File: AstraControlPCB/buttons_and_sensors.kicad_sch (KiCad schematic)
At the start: 11 parts, among them CN13 4P JST ZH, CN14 4P JST ZH, CN5 4P JST ZH

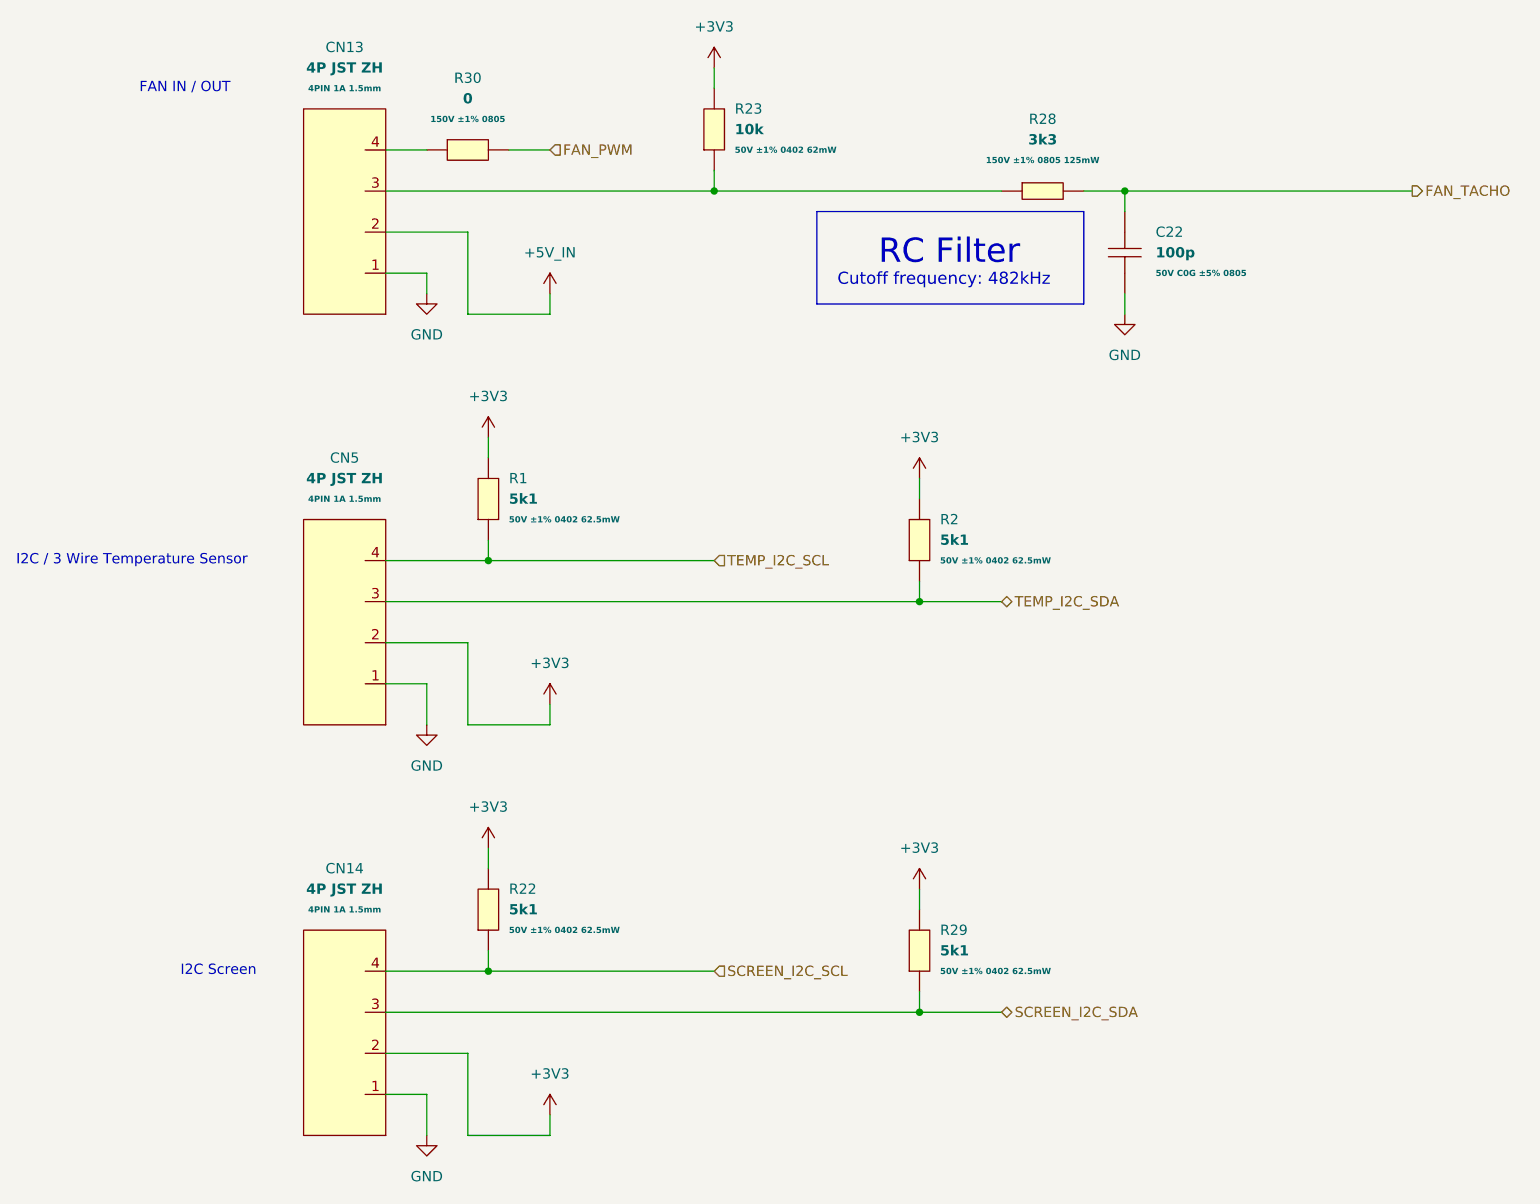
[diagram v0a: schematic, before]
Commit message: Remove plus minus symbol
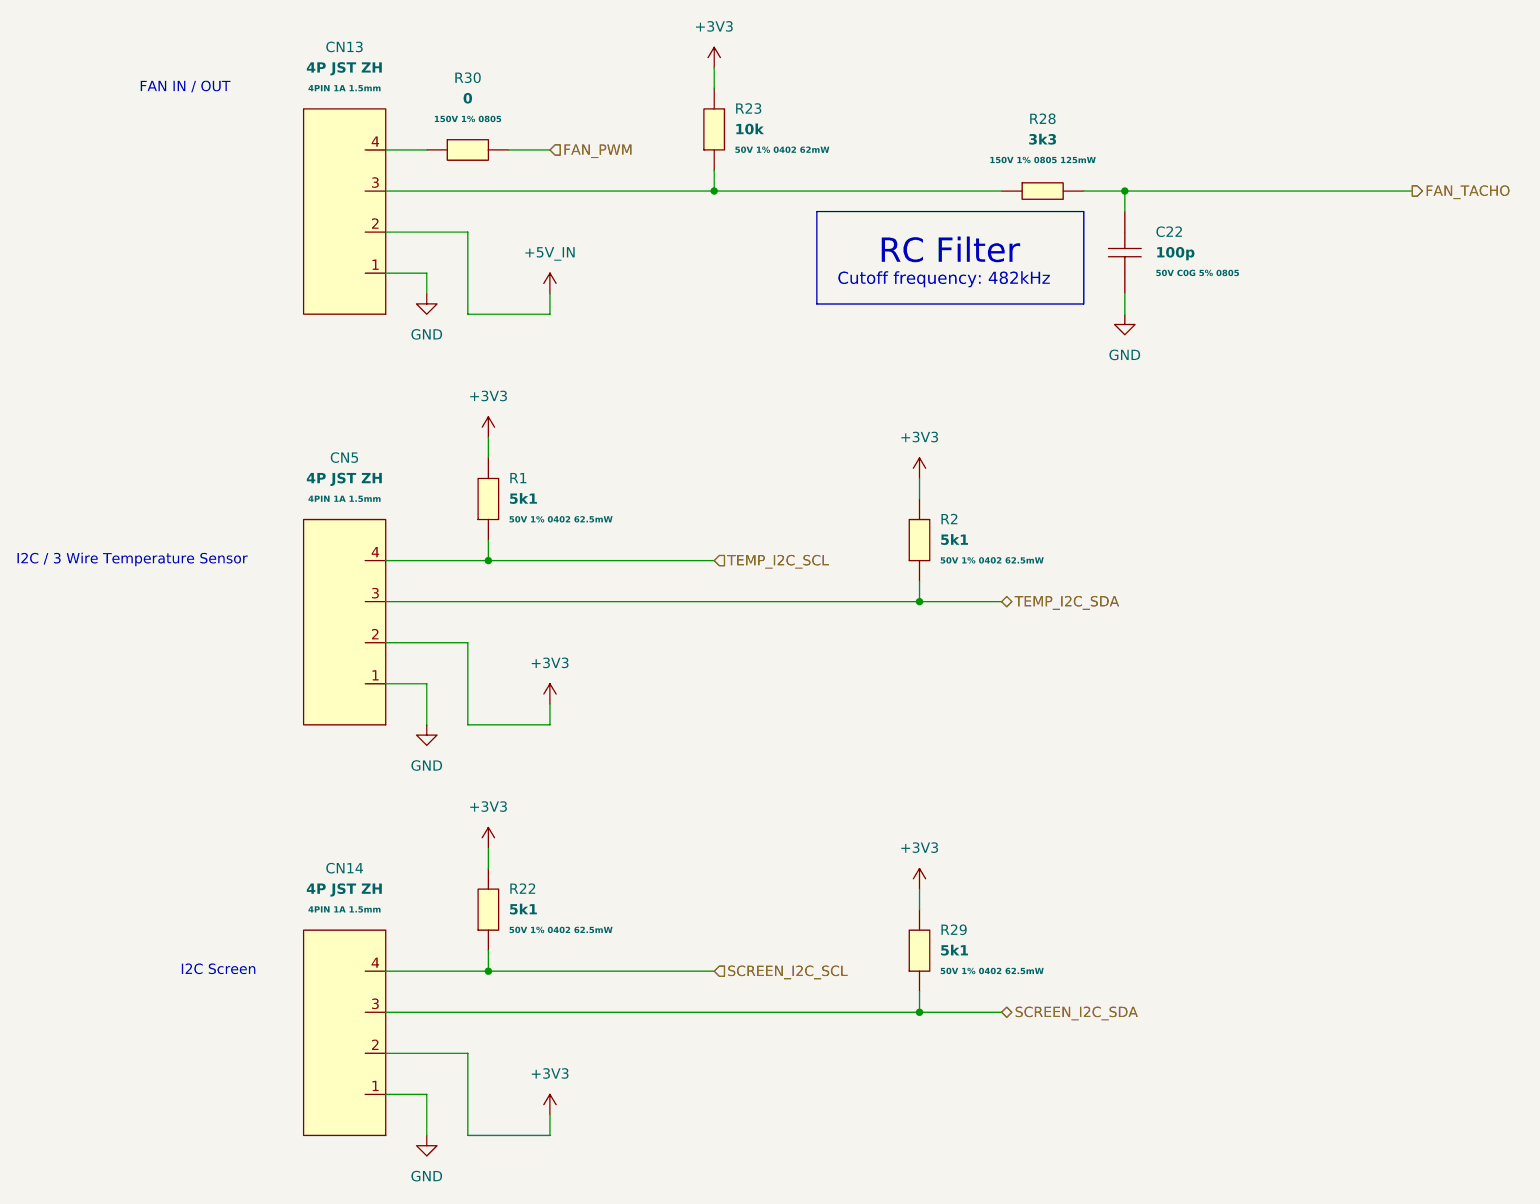
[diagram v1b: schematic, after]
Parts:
- C22: Extra Values 50V C0G ±5% 0805 -> 50V C0G 5% 0805
- R1, R2, R22, R29: Extra Values 50V ±1% 0402 62.5mW -> 50V 1% 0402 62.5mW
- R23: Extra Values 50V ±1% 0402 62mW -> 50V 1% 0402 62mW
- R28: Extra Values 150V ±1% 0805 125mW -> 150V 1% 0805 125mW
- R30: Extra Values 150V ±1% 0805 -> 150V 1% 0805
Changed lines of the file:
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@@
 			)
 		)
-		(property "Extra Values" "50V ±1% 0402 62.5mW "
+		(property "Extra Values" "50V 1% 0402 62.5mW "
 			(at 127 88.8999 90)
 			(effects
@@
 			)
 		)
-		(property "Extra Values" "50V ±1% 0402 62.5mW "
+		(property "Extra Values" "50V 1% 0402 62.5mW "
 			(at 180.34 93.9799 90)
 			(effects
@@
 			)
 		)
-		(property "Extra Values" "50V C0G ±5% 0805"
+		(property "Extra Values" "50V C0G 5% 0805"
 			(at 207.01 58.4199 90)
 			(effects
@@
 			)
 		)
-		(property "Extra Values" "50V ±1% 0402 62mW"
+		(property "Extra Values" "50V 1% 0402 62mW"
 			(at 154.94 43.1799 90)
 			(effects
@@
 			)
 		)
-		(property "Extra Values" "50V ±1% 0402 62.5mW "
+		(property "Extra Values" "50V 1% 0402 62.5mW "
 			(at 180.34 144.7799 90)
 			(effects
@@
 			)
 		)
-		(property "Extra Values" "50V ±1% 0402 62.5mW "
+		(property "Extra Values" "50V 1% 0402 62.5mW "
 			(at 127 139.6999 90)
 			(effects
@@
 			)
 		)
-		(property "Extra Values" " 150V ±1% 0805 125mW"
+		(property "Extra Values" " 150V 1% 0805 125mW"
 			(at 193.04 44.45 0)
 			(effects
@@
 			)
 		)
-		(property "Extra Values" "150V ±1% 0805"
+		(property "Extra Values" "150V 1% 0805"
 			(at 121.92 39.37 0)
 			(effects
